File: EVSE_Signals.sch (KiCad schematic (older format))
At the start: 26 parts, among them Q25 MMBT3904

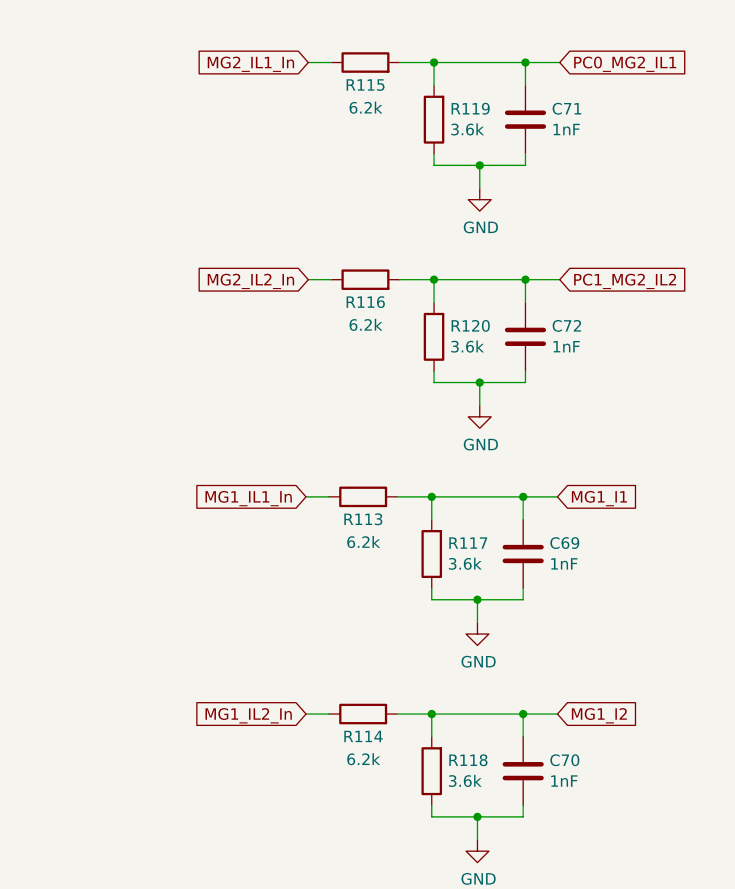
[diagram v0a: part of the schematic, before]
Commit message: corrected tracking error around MG1 and MG current sensors.  J7 footprint updated (J1 left unchanged as tracking layout is currently ok).
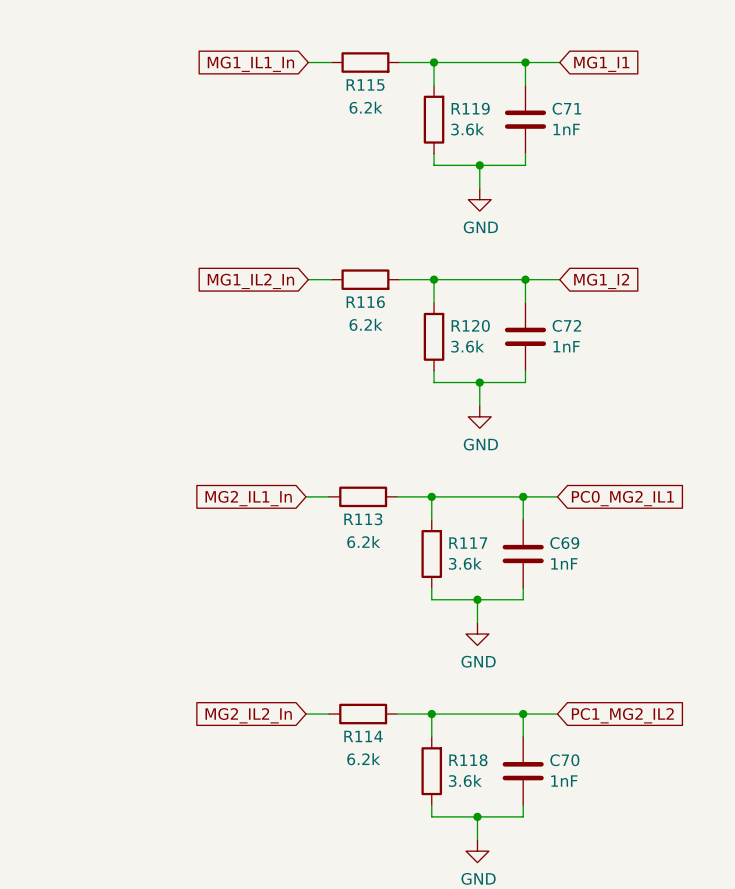
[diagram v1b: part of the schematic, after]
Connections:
- net MG1_I1: now also C71.1, R115.2, R119.2; no longer C69.1, R113.2, R117.2
- net MG1_I2: now also C72.1, R116.2, R120.2; no longer C70.1, R114.2, R118.2
- net MG1_IL1_In: now also R115.1; no longer R113.1
- net MG1_IL2_In: now also R116.1; no longer R114.1
- net MG2_IL1_In: now also R113.1; no longer R115.1
- net MG2_IL2_In: now also R114.1; no longer R116.1
- net PC0_MG2_IL1: now also C69.1, R113.2, R117.2; no longer C71.1, R115.2, R119.2
- net PC1_MG2_IL2: now also C70.1, R114.2, R118.2; no longer C72.1, R116.2, R120.2
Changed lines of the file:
@@
 $Descr A4 11693 8268
 encoding utf-8
-Sheet 8 8
+Sheet 5 8
 Title "DC Controller STM32"
-Date "2020-07-04"
-Rev "2"
+Date "2020-10-18"
+Rev "3"
 Comp ""
 Comment1 "Designed: A Martell"
@@
 Wire Wire Line
 	8470 1710 8670 1710
-Text GLabel 8820 1260 2    50   Input ~ 0
+Text GLabel 8810 3160 2    50   Input ~ 0
 PC0_MG2_IL1
 Wire Wire Line
 	8820 1260 8670 1260
 Connection ~ 8670 1260
-Text GLabel 7720 1260 0    50   Input ~ 0
+Text GLabel 7710 3160 0    50   Input ~ 0
 MG2_IL1_In
 Wire Wire Line
@@
 Wire Wire Line
 	8470 2660 8670 2660
-Text GLabel 8820 2210 2    50   Input ~ 0
+Text GLabel 8810 4110 2    50   Input ~ 0
 PC1_MG2_IL2
 Wire Wire Line
 	8820 2210 8670 2210
 Connection ~ 8670 2210
-Text GLabel 7720 2210 0    50   Input ~ 0
+Text GLabel 7710 4110 0    50   Input ~ 0
 MG2_IL2_In
 Wire Wire Line
@@
 Wire Wire Line
 	8460 3610 8660 3610
-Text GLabel 8810 3160 2    50   Input ~ 0
+Text GLabel 8820 1260 2    50   Input ~ 0
 MG1_I1
 Wire Wire Line
 	8810 3160 8660 3160
 Connection ~ 8660 3160
-Text GLabel 7710 3160 0    50   Input ~ 0
+Text GLabel 7720 1260 0    50   Input ~ 0
 MG1_IL1_In
 Wire Wire Line
@@
 Wire Wire Line
 	8460 4560 8660 4560
-Text GLabel 8810 4110 2    50   Input ~ 0
+Text GLabel 8820 2210 2    50   Input ~ 0
 MG1_I2
 Wire Wire Line
 	8810 4110 8660 4110
 Connection ~ 8660 4110
-Text GLabel 7710 4110 0    50   Input ~ 0
+Text GLabel 7720 2210 0    50   Input ~ 0
 MG1_IL2_In
 Wire Wire Line
